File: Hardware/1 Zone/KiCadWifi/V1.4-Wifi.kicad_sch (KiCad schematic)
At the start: 129 parts, among them CN11 Pinheader 1x02 P2.54 Horizont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, CN16 Pinheader 1x02 P2.54 Horizont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, Q1 AOD4184A, Q10 IRLML2502, Q11 SI2300, Q12 S8050, Q8 UMH3NTN, SW1 K2-1102DP-G3SW-04, SW2 K2-1102DP-G3SW-04, SW3 K2-1102DP-G3SW-04, SW4 K2-1102DP-G3SW-04, U1 POWER-JACK, U11 CH340C, U15 AMS1117-3.3, U16 MC34063ECD-TR, U17 LM4040DIM3-2.5+T, U18 ATMEGA4809-AFR, U2 AO4409, U20 ACS712ELCTR-20A-T, U22 CH340C, U4 AMS1117-5.0, U9 WT8266-S5ESP-12F

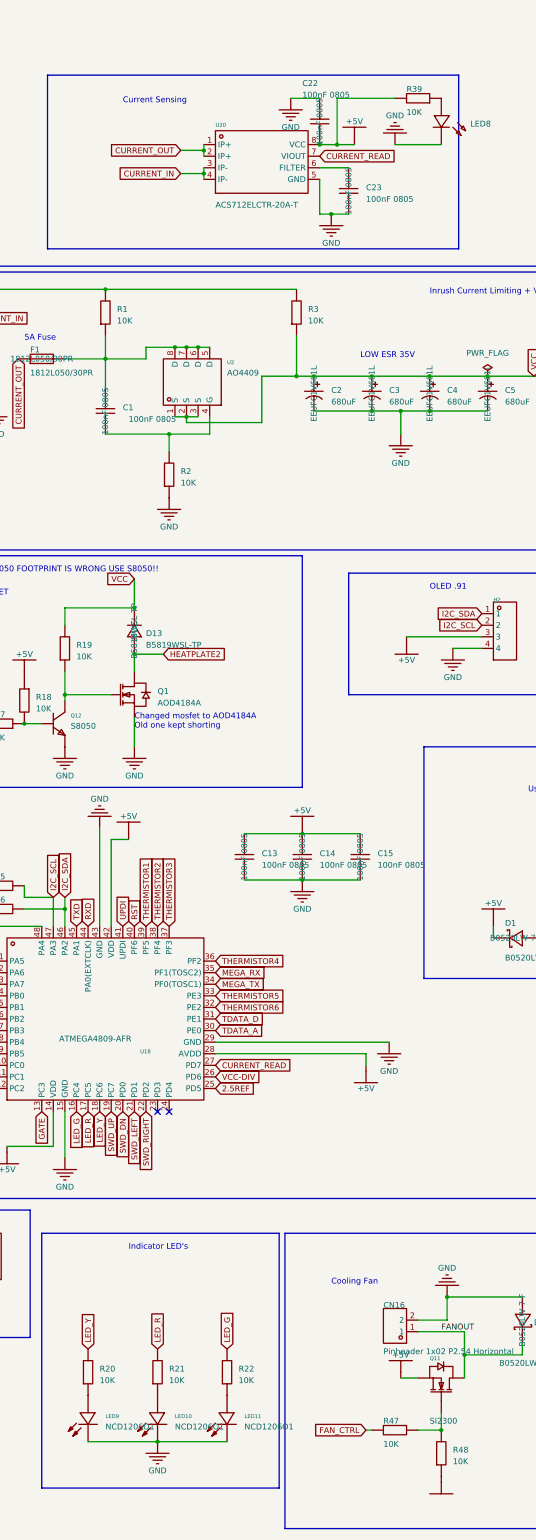
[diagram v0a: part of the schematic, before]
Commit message: Replaced part LED8-LED11
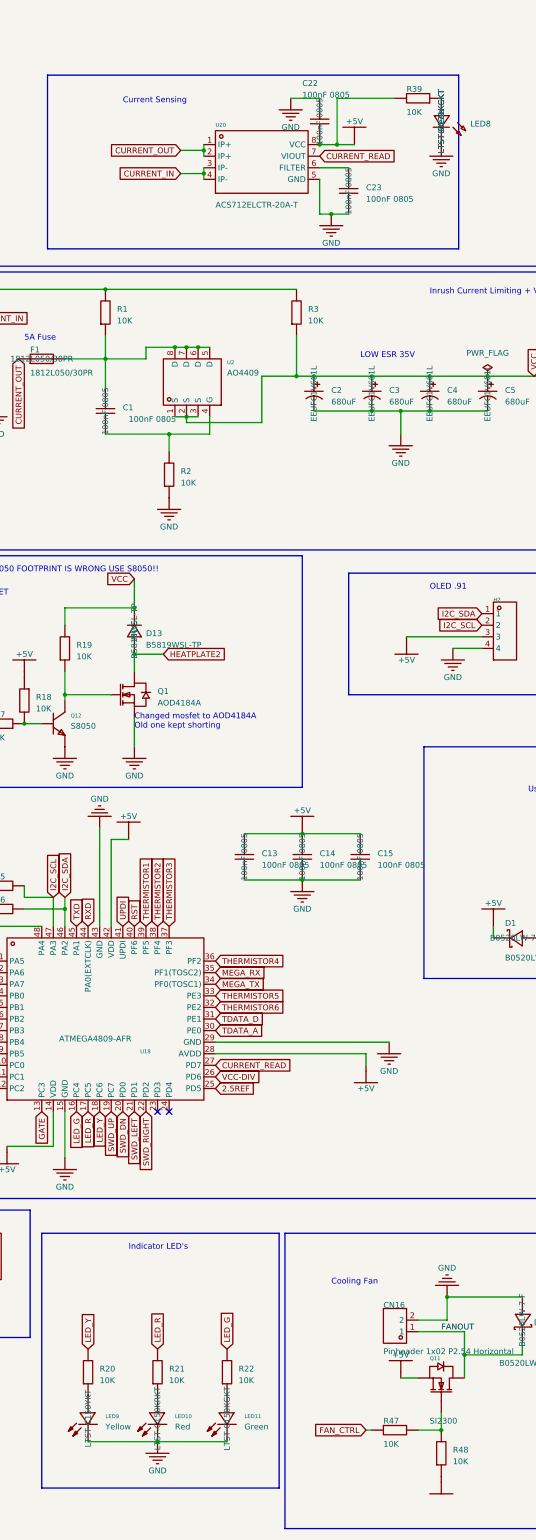
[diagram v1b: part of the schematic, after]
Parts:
- LED10: value NCD1206O1 -> Red; MPN (none) -> LTST-C150KRKT; Manufacturer 国星光电 -> Liteon; Manufacturer Part LED_R -> LTST-C150KRKT
- LED11: value NCD1206O1 -> Green; MPN (none) -> LTST-C150KGKT; Manufacturer 国星光电 -> Liteon; Manufacturer Part LED_G -> LTST-C150KGKT
- LED8: value ~ -> Green; MPN (none) -> LTST-C171KGKT; Manufacturer (none) -> Liteon; Manufacturer Part (none) -> LTST-C171KGKT
- LED9: value NCD1206O1 -> Yellow; MPN (none) -> LTST-C150YKT; Manufacturer 国星光电 -> Liteon; Manufacturer Part LED_Y -> LTST-C150YKT

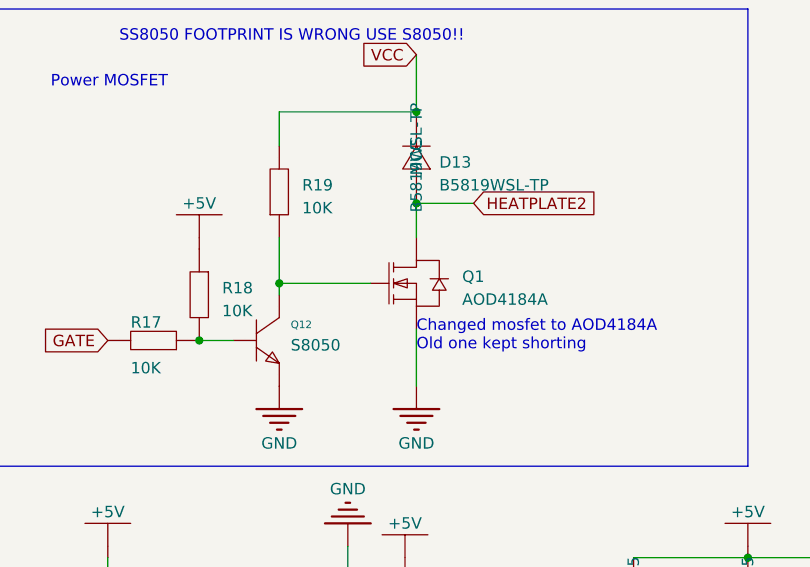
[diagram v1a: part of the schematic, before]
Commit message: Replaced part Q1 from AOD4184A to IPD90N04S403
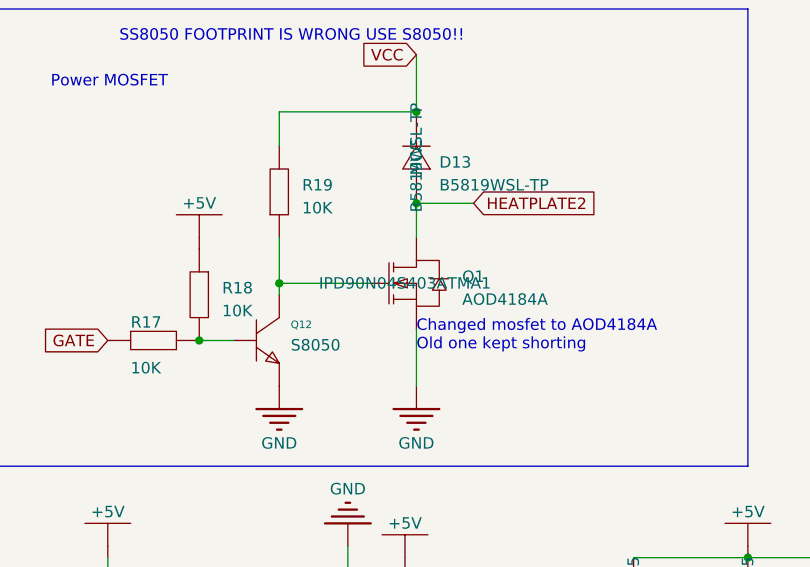
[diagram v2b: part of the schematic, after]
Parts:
- Q1: MPN (none) -> IPD90N04S403ATMA1; Manufacturer AOS -> Infineon; Manufacturer Part AOD4184A -> IPD90N04S403ATMA1

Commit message: Replaced part Q10 from IRLML2502 to PJA3404A. Updated footprint.
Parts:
- Q10: value IRLML2502 -> PJA3404A; footprint V1.4-Wifi-easyedapro:SOT-23_L2.9-W1.3-P1.90-LS2.4-BR -> Package_TO_SOT_SMD:SOT-23-3; MPN (none) -> PJA3404A_R1_00001; Manufacturer UMW(友台半导体) -> Panjit; Manufacturer Part IRLML2502 -> PJA3404A_R1_00001
- Q8: Manufacturer ROHM(罗姆) -> ROHM

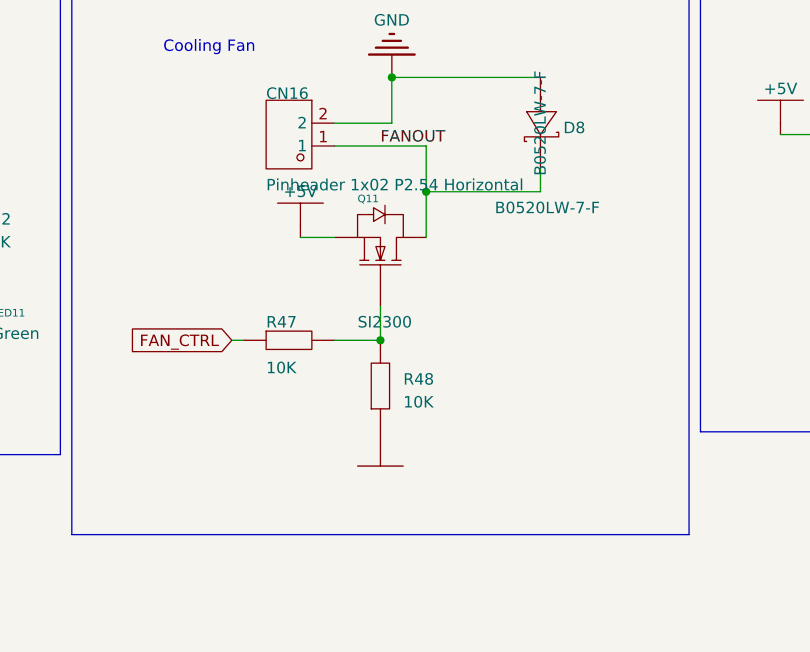
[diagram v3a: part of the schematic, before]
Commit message: Replaced part Q11 from SI2300 to PJA3404A to simplify BOM. Updated footprint.
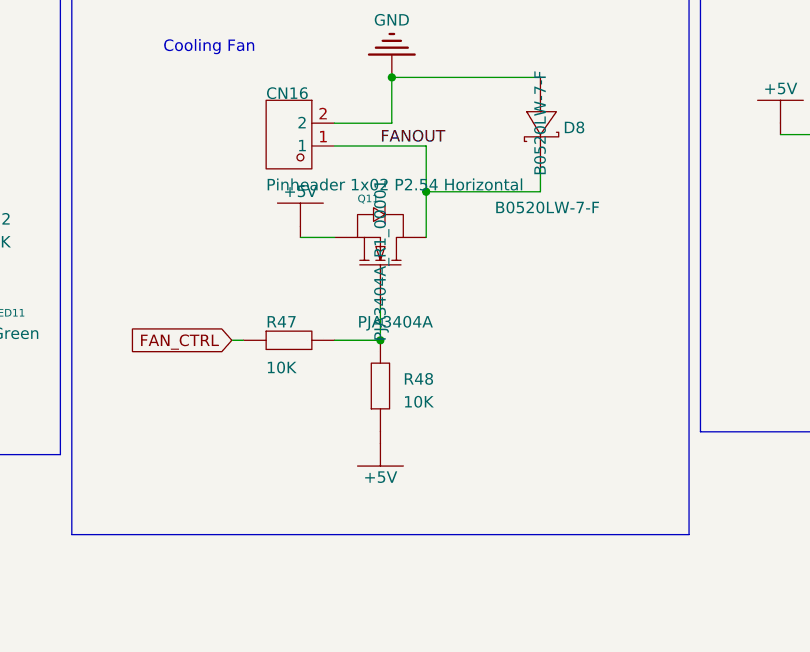
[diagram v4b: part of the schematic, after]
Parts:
- Q11: value SI2300 -> PJA3404A; footprint V1.4-Wifi-easyedapro:SOT-23-3_L2.9-W1.3-P0.95-LS2.4-BR -> Package_TO_SOT_SMD:SOT-23-3; MPN (none) -> PJA3404A_R1_00001; Manufacturer KUU -> Panjit; Manufacturer Part SI2300 -> PJA3404A_R1_00001
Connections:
- net +5V: now also R48.1

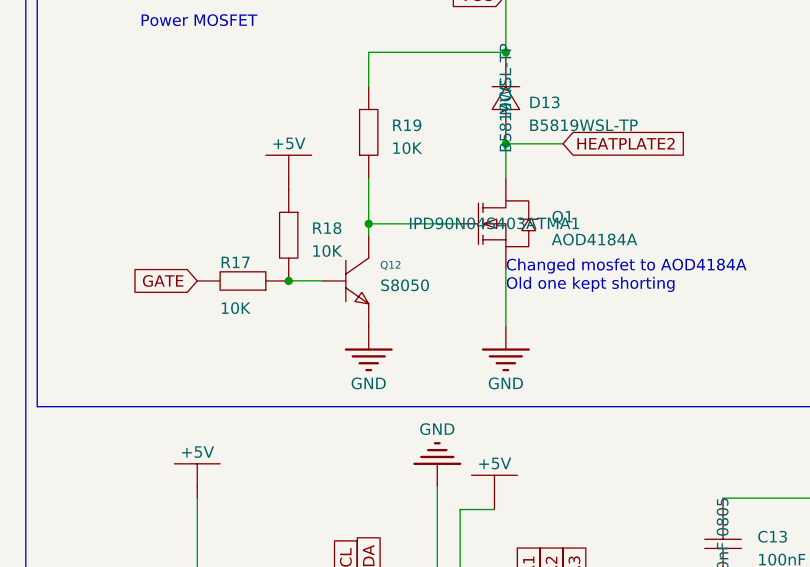
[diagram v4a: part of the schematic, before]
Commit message: Replaced part Q12 from S8050 to BC816-16VL. Updated footprint.
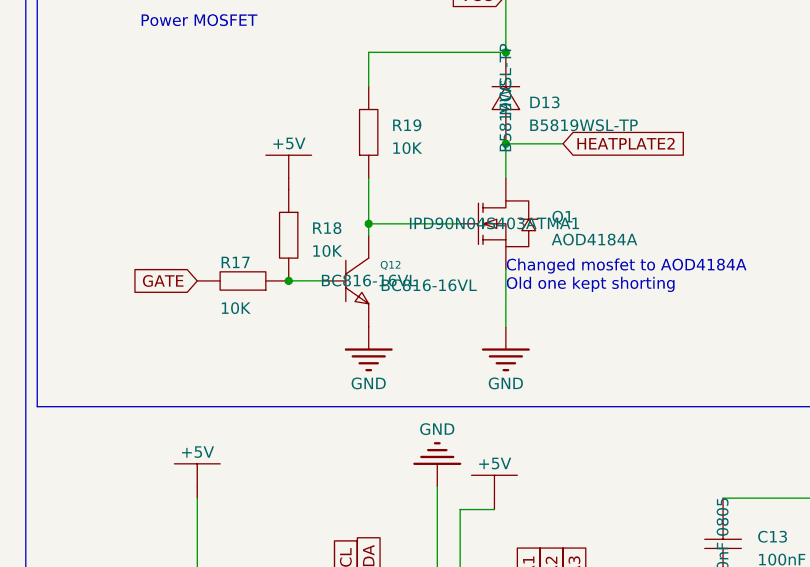
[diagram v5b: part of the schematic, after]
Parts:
- Q12: value S8050 -> BC816-16VL; footprint V1.4-Wifi-easyedapro:SOT-23-3_L2.9-W1.3-P1.90-LS2.4-BR -> Package_TO_SOT_SMD:SOT-23-3; MPN (none) -> BC816-16VL; Manufacturer JSMSEMI(杰盛微) -> Nexperia; Manufacturer Part S8050 -> BC816-16VL

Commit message: Adjusted resistor value to assist picking correct part by pcb supplier
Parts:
- R1, R15, R16, R17, R18, R19, R2, R20, R21, R22, R23, R24, R25, R26, R27, R28, R29, R3, R30, R31, R32, R33, R34, R35, R36, R37, R38, R39, R4, R40, R41, R42, R43, R44, R45, R46, R47, R48, R49, R5, R50, R51, R52, R53, R54, R55, R6, R7, R8: value 10K -> 10K 0603
- R10, R11, R12, R13, R14, R9: value 15kΩ -> 15K

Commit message: Fixed R and C values manually looking at EasyEDA editor
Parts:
- C23: value 100nF 0805 -> 1nF 0805
- C28: value 100nF 0805 -> 100nF 0603
- C6: value 100nF 0805 -> 220pF 0805
- C8: value 100nF 0805 -> 22uF 0805
- R1, R3: value 10K 0603 -> 47R 0805
- R11: value 15K -> 2K 0805
- R15, R16, R19, R23, R25, R26, R27, R28, R34, R4: value 10K 0603 -> 4K7 0805
- R17, R20, R21, R22, R5: value 10K 0603 -> 1K 0805
- R18, R2, R24, R29, R30, R31, R32, R33, R35, R36, R37, R38, R46, R48: value 10K 0603 -> 10K 0805
- R39, R44: value 10K 0603 -> 1K 0603
- R40: value 10K 0603 -> 750R 0805
- R45: value 10K 0603 -> 3K6 0603
- R47: value 10K 0603 -> 100R 0805
- R49, R52, R54: value 10K 0603 -> 15K 0805
- R51, R53: value 10K 0603 -> 2K 0805
- R6: value 10K 0603 -> .33R 0805
- R7: value 10K 0603 -> 7K5 0805
- R8: value 10K 0603 -> 1K5 0805
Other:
- note added: "Reference Voltage"
- note removed: "Refreance Voltage"
- moved on the sheet: R40

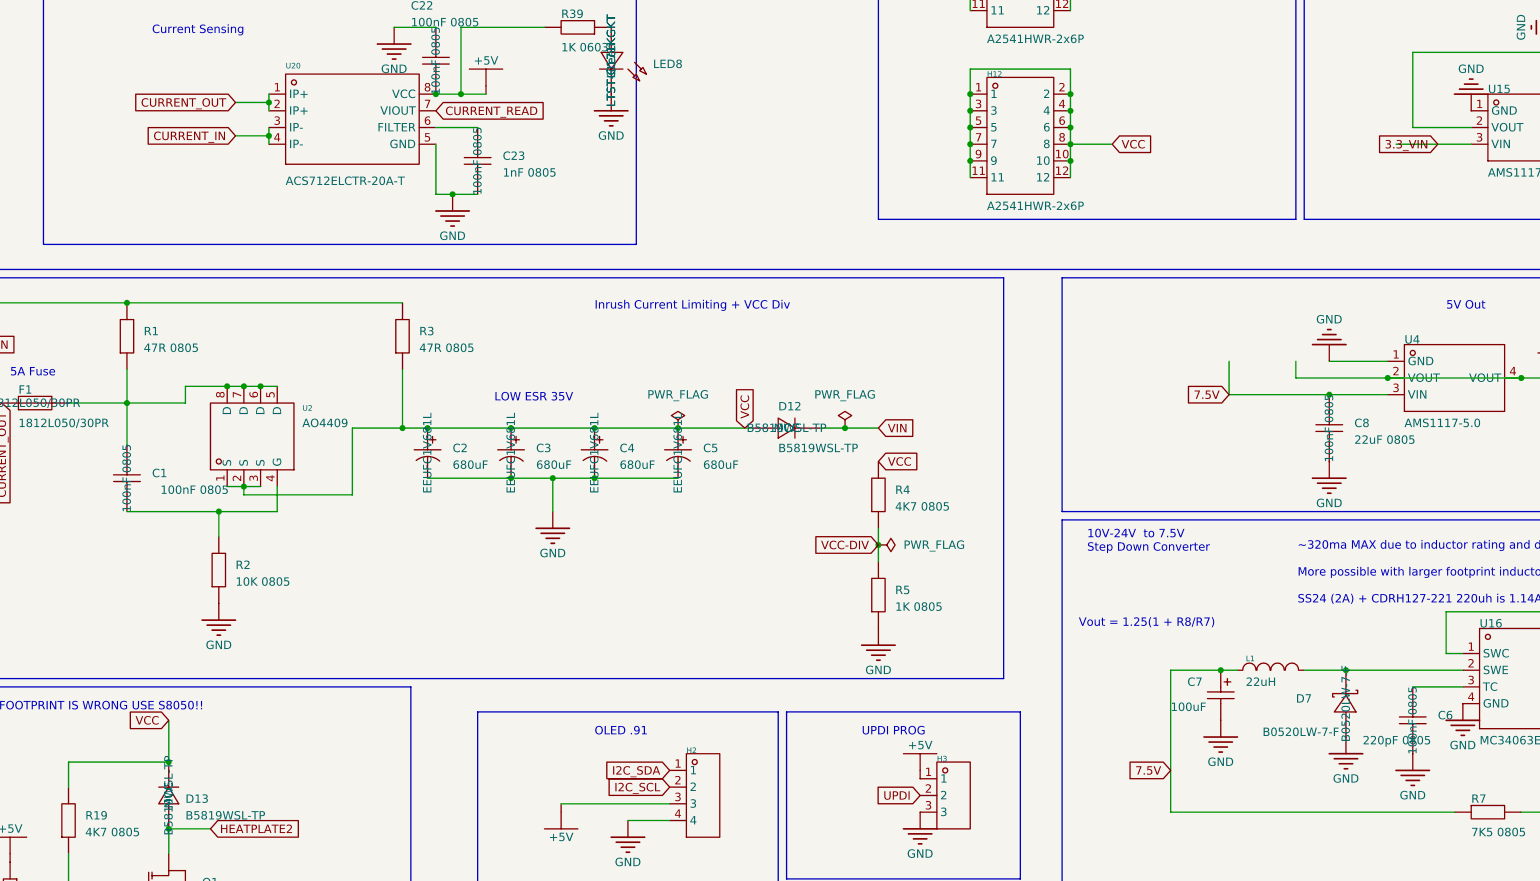
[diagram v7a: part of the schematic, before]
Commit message: Updated MPN for updated C parts
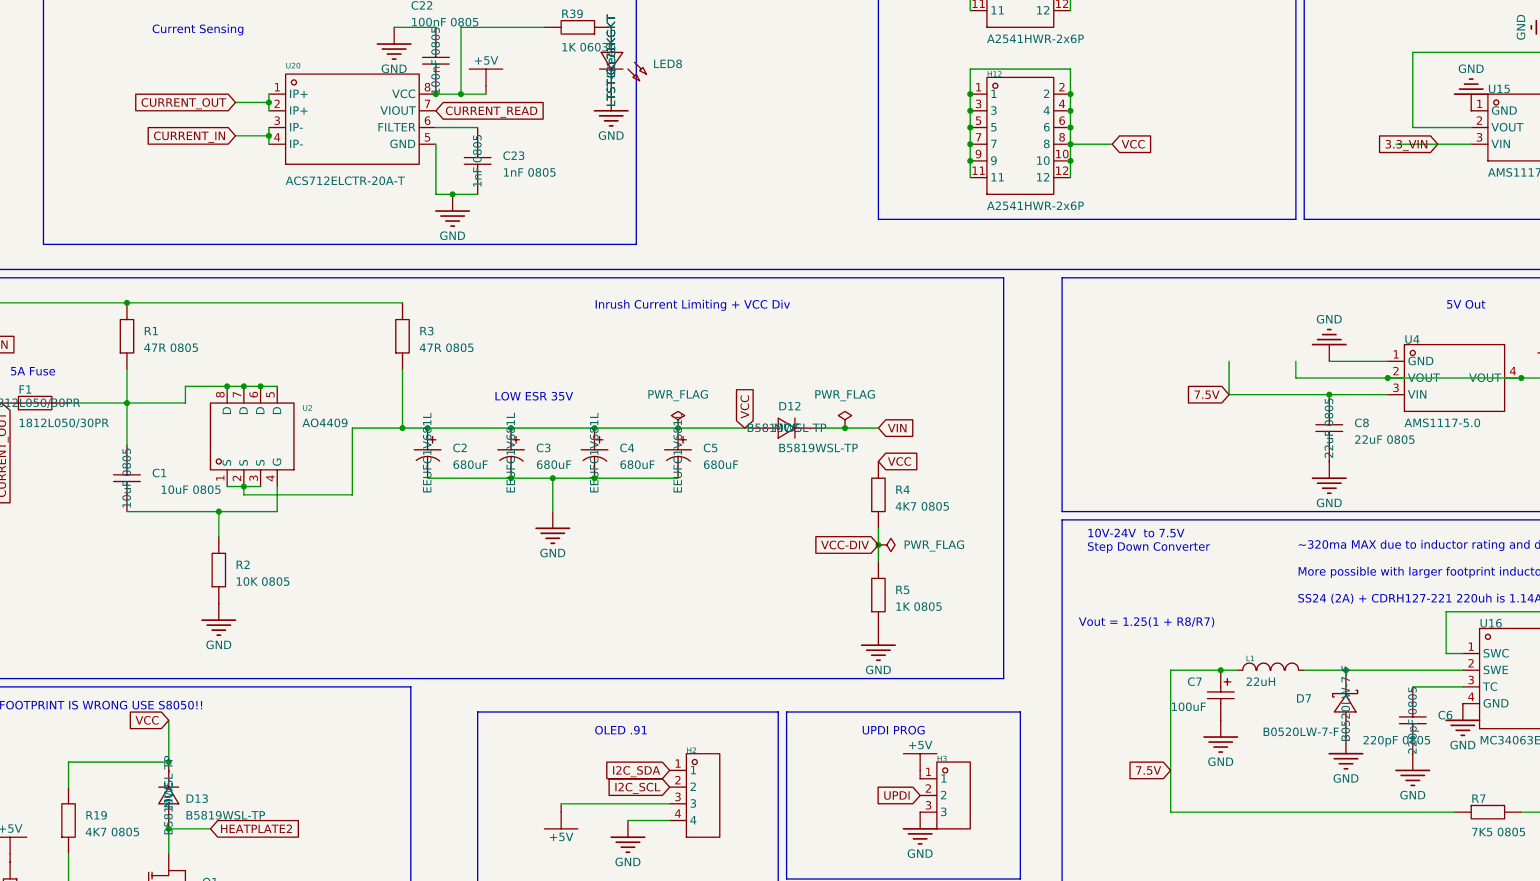
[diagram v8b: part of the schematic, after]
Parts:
- C1: value 100nF 0805 -> 10uF 0805; MPN 100nF 0805 -> 10uF 0805
- C23: MPN 100nF 0805 -> 1nF 0805
- C6: MPN 100nF 0805 -> 220pF 0805
- C8: MPN 100nF 0805 -> 22uF 0805
